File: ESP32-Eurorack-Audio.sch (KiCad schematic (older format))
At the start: 5 parts

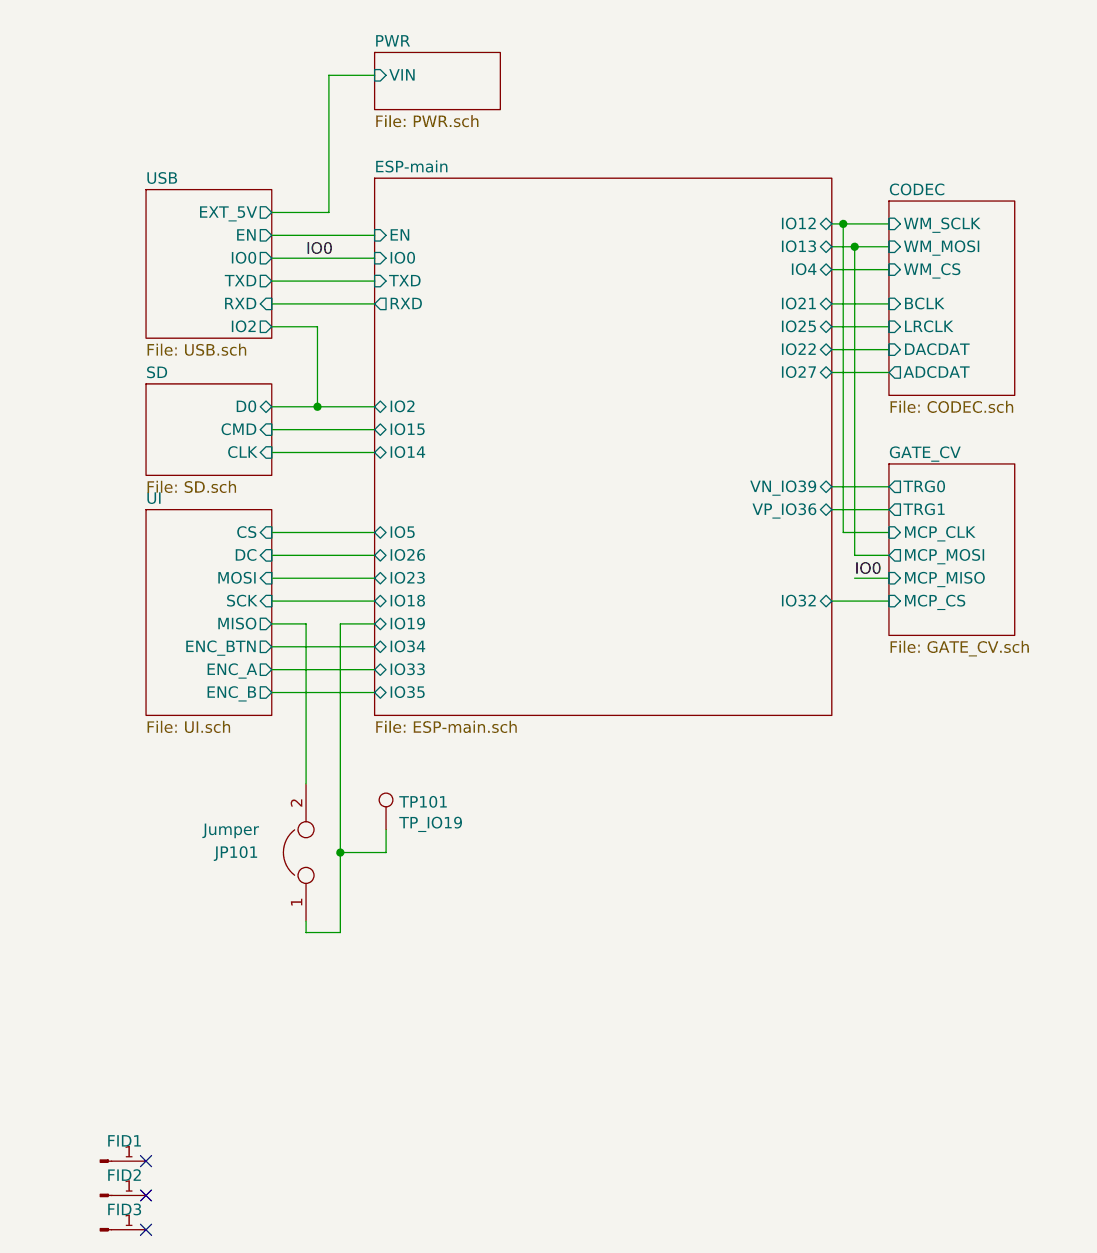
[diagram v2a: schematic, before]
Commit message: cleaned up schematic
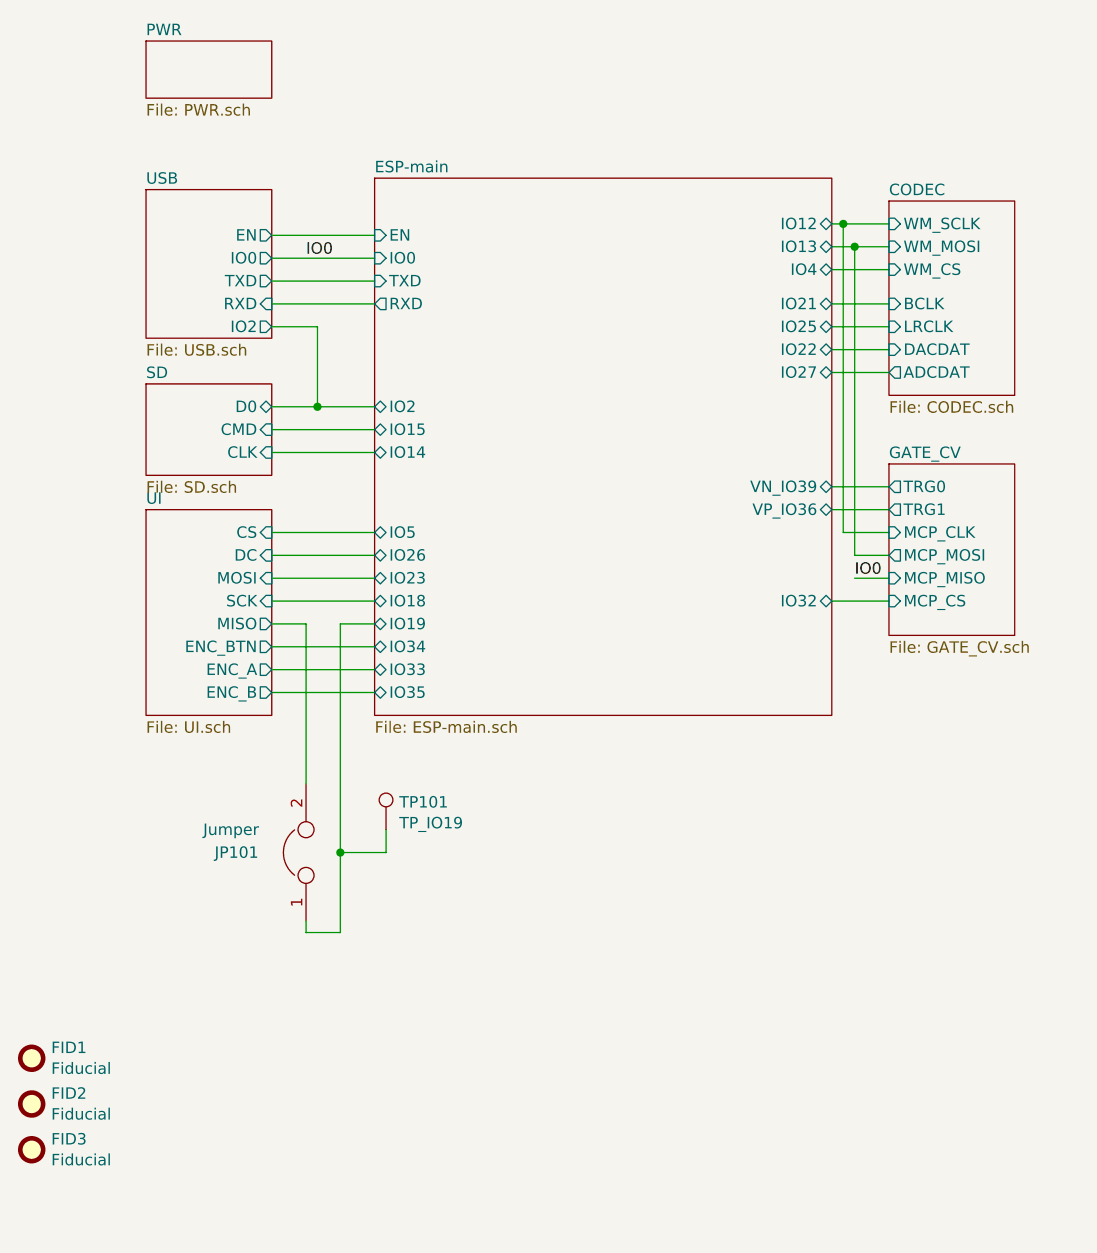
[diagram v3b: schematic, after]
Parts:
- removed FID1, FID2, FID3: ~, Fiducial:Fiducial_1mm_Dia_2.54mm_Outer_CopperTop, symbol Connector:Conn_01x01_Male
- added FID1, FID2, FID3: Fiducial, symbol Mechanical:Fiducial
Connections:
- no-connect marks 3 -> 0
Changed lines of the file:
@@
 Sheet 1 8
 Title "ESP32 Eurorack Audio Module"
-Date "2019-03-27"
-Rev "C"
+Date "2019-05-13"
+Rev "D"
 Comp "(c) Robert Manzke 2019"
 Comment1 "https://creativecommons.org/licenses/by-nc-sa/4.0/"
@@
 F0 "USB" 50
 F1 "USB.sch" 50
-F2 "EXT_5V" O R 2100 2600 50
-F3 "EN" O R 2100 2700 50
-F4 "IO0" O R 2100 2800 50
-F5 "TXD" O R 2100 2900 50
-F6 "RXD" I R 2100 3000 50
-F7 "IO2" O R 2100 3100 50
+F2 "EN" O R 2100 2700 50
+F3 "IO0" O R 2100 2800 50
+F4 "TXD" O R 2100 2900 50
+F5 "RXD" I R 2100 3000 50
+F6 "IO2" O R 2100 3100 50
 $EndSheet
 Wire Wire Line
@@
 	2100 4700 2550 4700
 $Sheet
-S 2550 1900 550  250
+S 1550 1850 550  250
 U 5B69D53C
 F0 "PWR" 50
 F1 "PWR.sch" 50
-F2 "VIN" I L 2550 2000 50
 $EndSheet
 $Sheet
@@
 F8 "ADCDAT" O L 4800 3300 50
 $EndSheet
-Wire Wire Line
-	2550 2000 2350 2000
-Wire Wire Line
-	2350 2000 2350 2600
-Wire Wire Line
-	2350 2600 2100 2600
 $Sheet
 S 4800 3700 550  750
@@
 Wire Wire Line
 	4650 2750 4550 2750
-$Comp
-L Connector:Conn_01x01_Male FID1
-U 1 1 5B6E15CE
-P 1350 6750
-F 0 "FID1" H 1456 6837 50  0000 C CNN
-F 1 "~" H 1456 6837 50  0000 C CNN
-F 2 "Fiducial:Fiducial_1mm_Dia_2.54mm_Outer_CopperTop" H 1350 6750 50  0001 C CNN
-F 3 "~" H 1350 6750 50  0001 C CNN
-	1    1350 6750
-	1    0    0    -1
-$EndComp
-$Comp
-L Connector:Conn_01x01_Male FID2
-U 1 1 5B6E1636
-P 1350 6900
-F 0 "FID2" H 1456 6987 50  0000 C CNN
-F 1 "~" H 1456 6987 50  0000 C CNN
-F 2 "Fiducial:Fiducial_1mm_Dia_2.54mm_Outer_CopperTop" H 1350 6900 50  0001 C CNN
-F 3 "~" H 1350 6900 50  0001 C CNN
-	1    1350 6900
-	1    0    0    -1
-$EndComp
-$Comp
-L Connector:Conn_01x01_Male FID3
-U 1 1 5B6E165A
-P 1350 7050
-F 0 "FID3" H 1456 7137 50  0000 C CNN
-F 1 "~" H 1456 7137 50  0000 C CNN
-F 2 "Fiducial:Fiducial_1mm_Dia_2.54mm_Outer_CopperTop" H 1350 7050 50  0001 C CNN
-F 3 "~" H 1350 7050 50  0001 C CNN
-	1    1350 7050
-	1    0    0    -1
-$EndComp
-NoConn ~ 1550 6750
-NoConn ~ 1550 6900
-NoConn ~ 1550 7050
 Text Label 4650 4200 0    50   ~ 0
 IO0
@@
 Wire Wire Line
 	2400 5400 2400 5750
+$Comp
+L Mechanical:Fiducial FID1
+U 1 1 5CD9B8CA
+P 1050 6300
+F 0 "FID1" H 1135 6346 50  0000 L CNN
+F 1 "Fiducial" H 1135 6255 50  0000 L CNN
+F 2 "" H 1050 6300 50  0001 C CNN
+F 3 "~" H 1050 6300 50  0001 C CNN
+	1    1050 6300
+	1    0    0    -1
+$EndComp
+$Comp
+L Mechanical:Fiducial FID2
+U 1 1 5CD9C1AA
+P 1050 6500
+F 0 "FID2" H 1135 6546 50  0000 L CNN
+F 1 "Fiducial" H 1135 6455 50  0000 L CNN
+F 2 "" H 1050 6500 50  0001 C CNN
+F 3 "~" H 1050 6500 50  0001 C CNN
+	1    1050 6500
+	1    0    0    -1
+$EndComp
+$Comp
+L Mechanical:Fiducial FID3
+U 1 1 5CD9C2A4
+P 1050 6700
+F 0 "FID3" H 1135 6746 50  0000 L CNN
+F 1 "Fiducial" H 1135 6655 50  0000 L CNN
+F 2 "" H 1050 6700 50  0001 C CNN
+F 3 "~" H 1050 6700 50  0001 C CNN
+	1    1050 6700
+	1    0    0    -1
+$EndComp
 $EndSCHEMATC

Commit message: added pcb fiducials, updated date
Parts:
- FID1, FID2, FID3: footprint (none) -> Fiducial:Fiducial_1mm_Mask2mm
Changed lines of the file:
@@
 Sheet 1 8
 Title "ESP32 Eurorack Audio Module"
-Date "2019-05-13"
+Date "2019-06-13"
 Rev "D"
 Comp "(c) Robert Manzke 2019"
@@
 F 0 "FID1" H 1135 6346 50  0000 L CNN
 F 1 "Fiducial" H 1135 6255 50  0000 L CNN
-F 2 "" H 1050 6300 50  0001 C CNN
+F 2 "Fiducial:Fiducial_1mm_Mask2mm" H 1050 6300 50  0001 C CNN
 F 3 "~" H 1050 6300 50  0001 C CNN
 	1    1050 6300
@@
 F 0 "FID2" H 1135 6546 50  0000 L CNN
 F 1 "Fiducial" H 1135 6455 50  0000 L CNN
-F 2 "" H 1050 6500 50  0001 C CNN
+F 2 "Fiducial:Fiducial_1mm_Mask2mm" H 1050 6500 50  0001 C CNN
 F 3 "~" H 1050 6500 50  0001 C CNN
 	1    1050 6500
@@
 F 0 "FID3" H 1135 6746 50  0000 L CNN
 F 1 "Fiducial" H 1135 6655 50  0000 L CNN
-F 2 "" H 1050 6700 50  0001 C CNN
+F 2 "Fiducial:Fiducial_1mm_Mask2mm" H 1050 6700 50  0001 C CNN
 F 3 "~" H 1050 6700 50  0001 C CNN
 	1    1050 6700
